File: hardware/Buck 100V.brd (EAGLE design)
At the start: 100 x 80 mm, 31 parts, among them M1 SI3430DV, M2 SI5435BDC, Q1 FMMT625, Q2 FMMT723, U1 LT3756EMSE

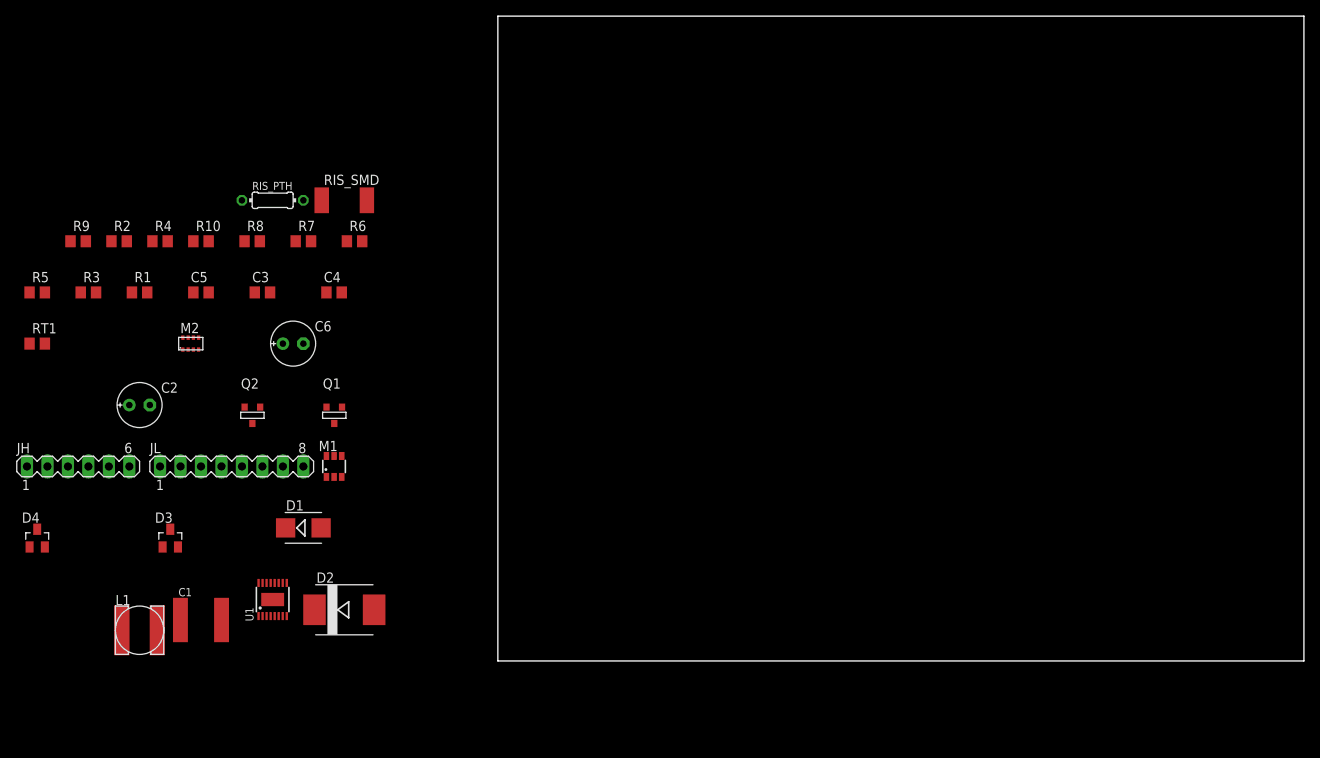
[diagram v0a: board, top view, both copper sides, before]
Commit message: Create kelvin terminated versions of current sense resistors and adjust schematic accordingly. Signals on the buck headers are now more clearly named. The kelvin terminated resistors WILL cause DRC errors on the board due to overlapping vias / pads but these can be safely ignored. Someday perhaps Eagle will get a better way to deal with kelvin termination.
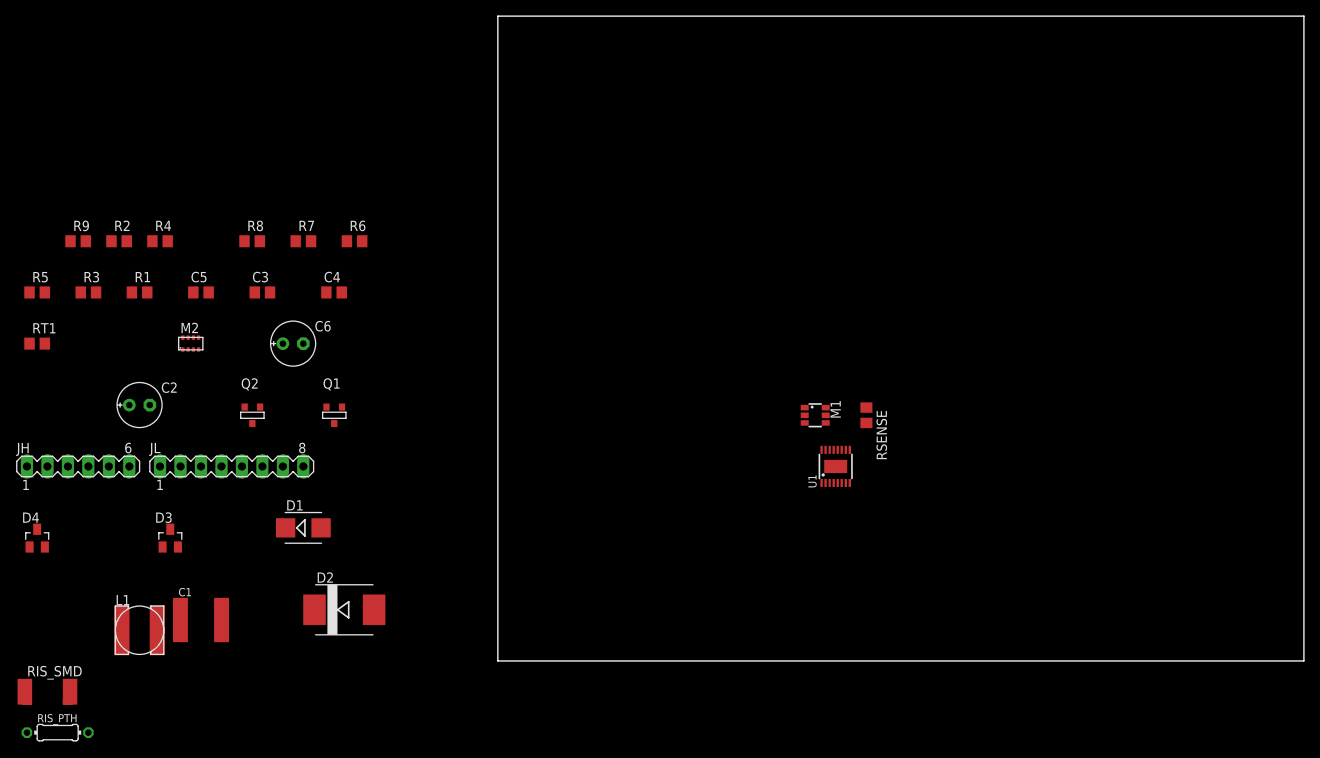
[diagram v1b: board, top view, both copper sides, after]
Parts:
- removed R10: 0.1, rcl:R0805
- added RSENSE: 0.1, rcl:R0805
- RIS_PTH: device rcl:0204/7 -> LED-drivers:0204/7-KELVIN
- RIS_SMD: device rcl:R2512 -> LED-drivers:R2512_KELVIN
- moved U1 71.8 mm to (41.9, 24.1)
- moved RIS_PTH 71.2 mm to (-54.6, -8.89)
- moved RIS_SMD 71.2 mm to (-55.9, -3.81)
- moved M1 60.0 mm to (39.4, 30.5), turned to 270 degrees
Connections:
- removed net IS: JH.3, M2.5, RIS_PTH.1, RIS_SMD.1, U1.3
- new net ISN: JH.3, RIS_PTH.1S, RIS_SMD.1S, U1.3
- new net ISP: JH.2, RIS_PTH.2S, RIS_SMD.2S, U1.4
- new net N$7: M2.5, RIS_PTH.1, RIS_SMD.1
- net GND: now also RSENSE.1; no longer R10.1
- net N$14: now also RSENSE.2; no longer R10.2
- net V+: no longer JH.2, U1.4

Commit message: Very rough initial board layout. Can now safely say that the board will be smaller than 2 inches by 3 inches.
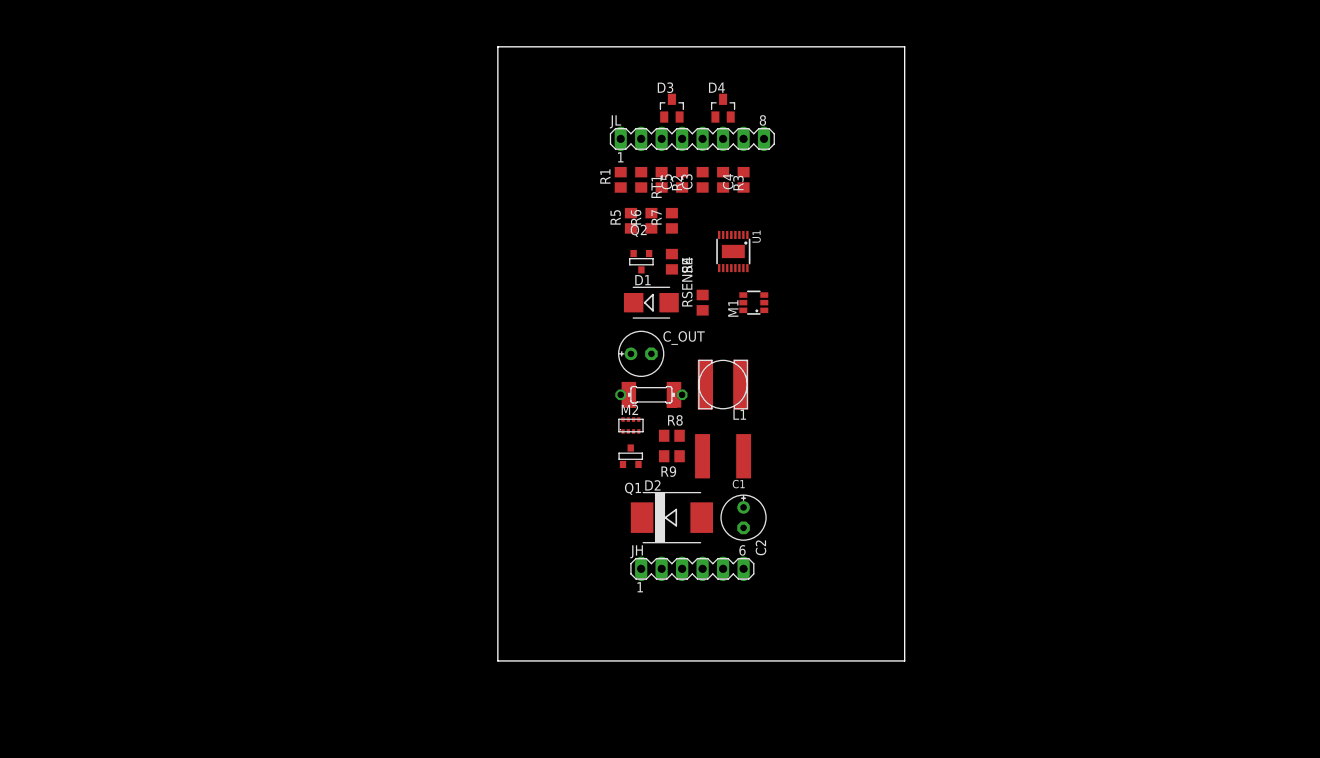
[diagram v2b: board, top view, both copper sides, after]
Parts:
- removed C6: 15uF 100V, rcl:E2,5-6E
- added C_OUT: 15uF 100V, rcl:E2,5-6E
- moved D4 100.4 mm to (27.9, 68.6)
- moved RIS_PTH 84.7 mm to (19.1, 33.0)
- moved RIS_SMD 83.5 mm to (19.1, 33.0)
- moved D3 82.0 mm to (21.6, 68.6)
- moved R3 80.0 mm to (27.9, 59.7), turned to 270 degrees
- moved L1 78.5 mm to (27.9, 34.3), turned to 180 degrees
- moved R9 78.3 mm to (21.6, 25.4), turned to 180 degrees
- moved RT1 77.6 mm to (17.8, 59.7), turned to 270 degrees
- moved JH 77.3 mm to (24.1, 11.4)
- moved C2 76.2 mm to (30.5, 17.8), turned to 270 degrees
- moved R5 74.2 mm to (16.5, 54.6), turned to 90 degrees
- moved JL 70.1 mm to (24.1, 64.8)
- moved C1 67.9 mm to (27.9, 25.4), turned to 180 degrees
- moved R2 67.7 mm to (20.3, 59.7), turned to 270 degrees
- moved R4 63.6 mm to (21.6, 49.5), turned to 270 degrees
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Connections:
- net N$12 renamed N_BUCK
- net LED_C: now also C_OUT.+; no longer C6.+
- net V+: now also C_OUT.-; no longer C6.-
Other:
- board size 100 x 80 mm -> 50.5 x 76.2 mm

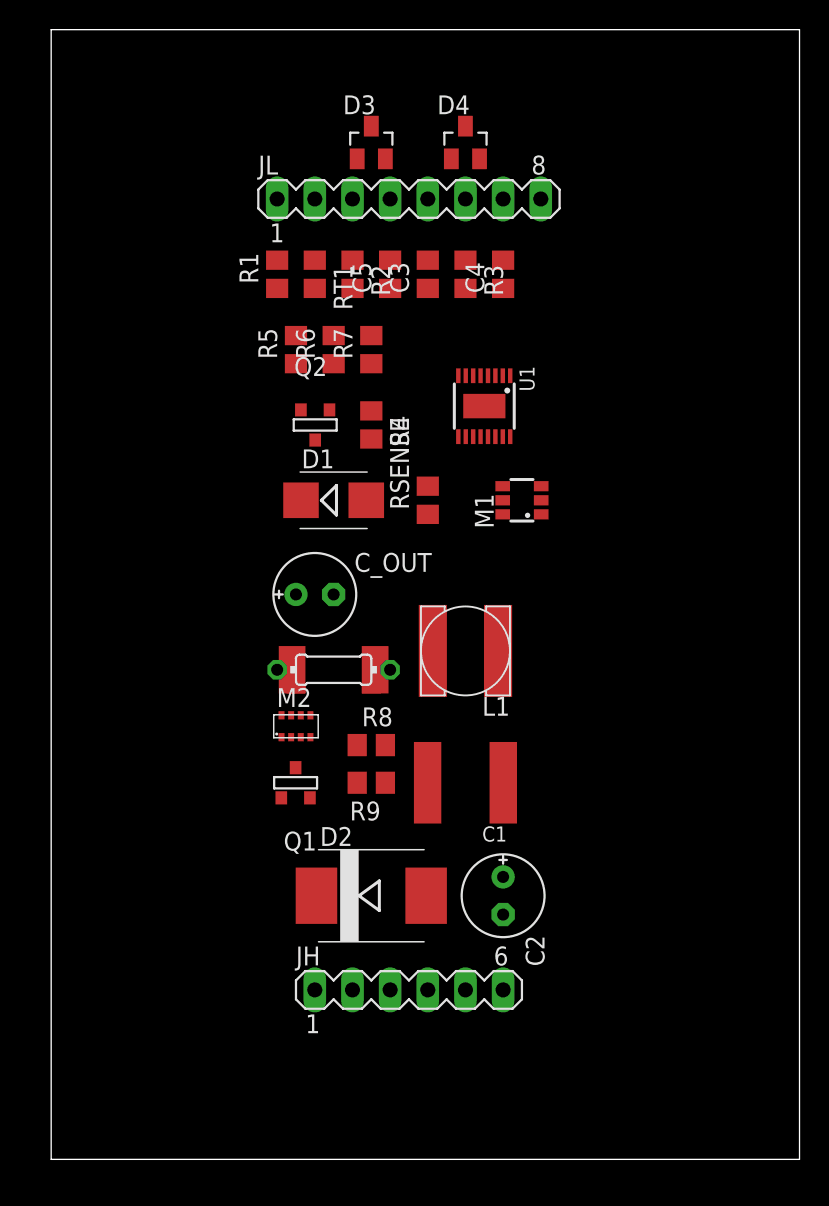
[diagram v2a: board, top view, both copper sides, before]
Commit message: Some progress on layout and routing.
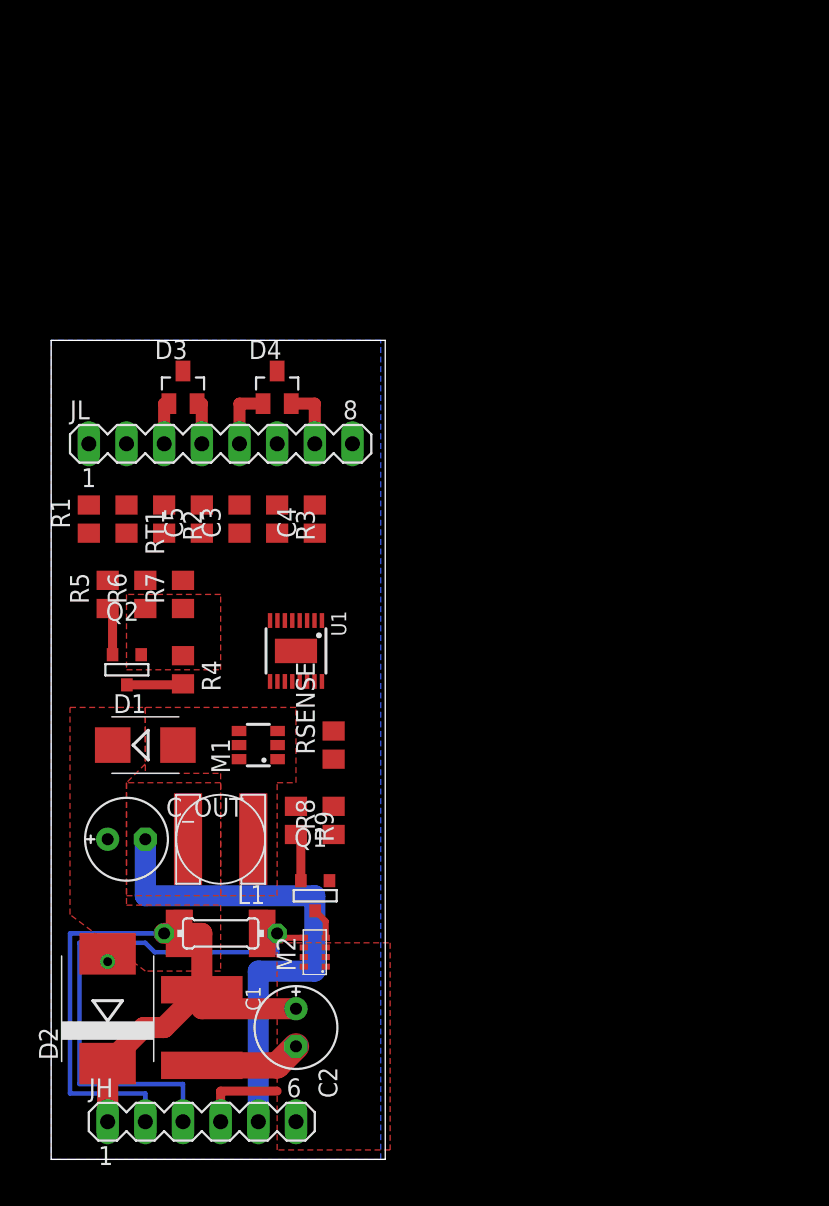
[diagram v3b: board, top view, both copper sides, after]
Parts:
- moved C1 24.3 mm to (10.2, 8.89), turned to 270 degrees
- moved M1 24.3 mm to (14.0, 27.9)
- moved C_OUT 20.8 mm to (5.08, 21.6)
- moved D1 20.8 mm to (6.35, 27.9)
- moved D4 20.8 mm to (15.2, 52.1)
- moved L1 20.8 mm to (11.4, 21.6)
- moved Q2 20.8 mm to (5.08, 33.0)
- moved R3 20.8 mm to (15.2, 43.2)
- moved R5 20.8 mm to (3.81, 38.1)
- moved R6 20.8 mm to (6.35, 38.1)
- moved RT1 20.8 mm to (5.08, 43.2)
- moved C3 20.8 mm to (12.7, 43.2)
- moved C4 20.8 mm to (17.8, 43.2)
- moved C5 20.8 mm to (10.2, 43.2)
- moved D3 20.8 mm to (8.89, 52.1)
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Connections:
- net LED_C: now also C_OUT.-; no longer C_OUT.+
- net V+: now also C_OUT.+; no longer C_OUT.-
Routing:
- net ISN: track 0.00 -> 36.5 mm
- net LED_C: track 0.00 -> 34.3 mm
- net ISP: track 0.00 -> 26.7 mm
- net V+: track 0.00 -> 26.3 mm
- net FB: track 0.00 -> 8.11 mm
- net GND: track 0.00 -> 7.41 mm, vias 0 -> 1
- net LED_A: track 0.00 -> 5.87 mm
- net CTRL: track 0.00 -> 4.30 mm
- net N$10: track 0.00 -> 3.25 mm
- net FB_TOP: track 0.00 -> 3.25 mm
- net N$7: track 0.00 -> 3.11 mm
- net PWM: track 0.00 -> 3.03 mm
- net /OPEN_LED: track 0.00 -> 3.03 mm
- net N$9: track 0.00 -> 2.11 mm
- added copper zone on layer 16, net GND
- added copper zone on layer 1, net LED_A
- added copper zone on layer 1, net LED_C
- added copper zone on layer 1, net N$8
- added copper zone on layer 1, net N_BUCK
- added copper zone on layer 1, net V+
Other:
- board size 50.5 x 76.2 mm -> 22.5 x 55.2 mm

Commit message: Progress on layout and routing.
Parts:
- moved M2 8.98 mm to (8.89, 12.7), turned to 180 degrees
- moved RIS_PTH 8.35 mm to (3.17, 14.0), turned to 90 degrees
- moved RIS_SMD 8.35 mm to (3.17, 14.0), turned to 90 degrees
- moved C1 8.13 mm to (16.5, 3.81), turned to 0 degrees
- moved JH 7.41 mm to (14.0, 8.89)
- moved D2 6.84 mm to (6.35, 3.81), turned to 0 degrees
- moved C2 5.12 mm to (19.1, 13.3), turned to 315 degrees
- moved L1 1.91 mm to (11.4, 19.7)
- moved M1 1.27 mm to (14.0, 26.7)
- moved R8 1.27 mm to (19.1, 21.6)
- moved R9 1.27 mm to (16.5, 21.6)
- moved RSENSE 1.27 mm to (19.1, 26.7)
- moved U1 0.63 mm to (16.5, 34.9)
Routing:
- net VREF: track 0.00 -> 43.8 mm, vias 0 -> 1
- net V+: track 26.3 -> 69.7 mm, vias 0 -> 4
- net N$11: track 0.00 -> 23.5 mm
- net FB_TOP: track 3.25 -> 24.6 mm, vias 0 -> 1
- net GND: track 7.41 -> 25.0 mm, vias 1 -> 13
- net FB: track 8.11 -> 24.4 mm
- net CTRL: track 4.30 -> 20.5 mm
- net N$14: track 0.00 -> 14.4 mm, vias 0 -> 2
- net N$9: track 2.11 -> 16.3 mm
- net LED_C: track 34.3 -> 47.6 mm, vias 0 -> 1
- net N$13: track 0.00 -> 7.02 mm
- net LED_A: track 5.87 -> 0.00 mm
- net ISN: track 36.5 -> 41.9 mm
- net N$7: track 3.11 -> 8.02 mm
- net ISP: track 26.7 -> 28.2 mm
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
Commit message: Checkpoint before trying autorouting again.
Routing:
- net FB: track 24.4 -> 44.5 mm, vias 0 -> 2
- net ISN: track 41.9 -> 51.8 mm, vias 0 -> 1
- net ISP: track 28.2 -> 37.0 mm, vias 0 -> 1
- net V+: track 69.7 -> 74.2 mm
- net LED_C: track 47.6 -> 50.8 mm
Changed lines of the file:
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@@
 <polygon width="0.4064" layer="1" thermals="no" rank="3">
 <vertex x="7.62" y="40.005"/>
-<vertex x="7.62" y="25.4"/>
-<vertex x="5.08" y="25.4"/>
+<vertex x="7.62" y="24.765"/>
+<vertex x="5.08" y="24.765"/>
 <vertex x="5.08" y="13.335"/>
 <vertex x="0" y="13.335"/>
@@
 <vertex x="13.97" y="15.875"/>
 </polygon>
+<wire x1="3.81" y1="21.59" x2="3.175" y2="21.59" width="1.6764" layer="1"/>
+<wire x1="3.175" y1="21.59" x2="3.175" y2="17.78" width="1.6764" layer="1"/>
 </signal>
 <signal name="SHDN">
@@
 <wire x1="21.2725" y1="38.1" x2="17.76" y2="38.1" width="0.3048" layer="1"/>
 <wire x1="17.76" y1="38.1" x2="17.76" y2="36.975" width="0.3048" layer="1"/>
-<wire x1="8.89" y1="32.07" x2="17.76" y2="36.975" width="0" layer="19" extent="1-1"/>
+<wire x1="8.89" y1="32.07" x2="11.115" y2="29.845" width="0.3048" layer="1"/>
+<wire x1="11.115" y1="29.845" x2="12.7" y2="29.845" width="0.3048" layer="1"/>
+<via x="12.7" y="29.845" extent="1-16" drill="0.6"/>
+<wire x1="12.7" y1="29.845" x2="19.3675" y2="29.845" width="0.3048" layer="16"/>
+<wire x1="19.3675" y1="29.845" x2="19.3675" y2="35.2425" width="0.3048" layer="16"/>
+<via x="19.3675" y="35.2425" extent="1-16" drill="0.6"/>
+<wire x1="19.3675" y1="35.2425" x2="19.3675" y2="36.068" width="0.254" layer="1"/>
+<wire x1="19.3675" y1="36.068" x2="17.78" y2="36.068" width="0.254" layer="1"/>
+<wire x1="17.78" y1="36.975" x2="17.78" y2="36.068" width="0.254" layer="1"/>
+<wire x1="17.78" y1="36.975" x2="17.76" y2="36.975" width="0" layer="19" extent="1-1"/>
 </signal>
 <signal name="FB_TOP">
@@
 <wire x1="10.4775" y1="39.05" x2="10.4775" y2="39.0525" width="0.3048" layer="1"/>
 <via x="10.4775" y="39.0525" extent="1-16" drill="0.6"/>
-<wire x1="10.4775" y1="39.0525" x2="2.8575" y2="39.0525" width="0.3048" layer="16"/>
-<wire x1="2.8575" y1="39.0525" x2="2.8575" y2="23.8125" width="0.3048" layer="16"/>
-<wire x1="2.8575" y1="23.8125" x2="6.35" y2="23.8125" width="0.3048" layer="16"/>
+<wire x1="10.4775" y1="39.0525" x2="1.27" y2="39.0525" width="0.3048" layer="16"/>
+<wire x1="1.27" y1="39.0525" x2="1.27" y2="23.8125" width="0.3048" layer="16"/>
+<wire x1="1.27" y1="23.8125" x2="6.35" y2="23.8125" width="0.3048" layer="16"/>
 <wire x1="6.35" y1="23.8125" x2="6.35" y2="21.59" width="0.3048" layer="16"/>
 </signal>
@@
 <wire x1="8.89" y1="12.065" x2="3.175" y2="17.78" width="0.3048" layer="16"/>
 <wire x1="4.445" y1="16.51" x2="3.175" y2="17.78" width="0.3048" layer="1"/>
-<wire x1="3.175" y1="17.78" x2="3.175" y2="18.0975" width="0.254" layer="16"/>
-<wire x1="3.175" y1="18.0975" x2="1.905" y2="19.3675" width="0.254" layer="16"/>
-<wire x1="1.905" y1="19.3675" x2="1.905" y2="31.115" width="0.254" layer="16"/>
-<wire x1="1.905" y1="31.115" x2="16.76" y2="36.975" width="0" layer="19" extent="1-16"/>
+<wire x1="3.175" y1="17.78" x2="1.905" y2="17.78" width="0.254" layer="1"/>
+<wire x1="1.905" y1="17.78" x2="1.905" y2="29.5275" width="0.254" layer="1"/>
+<wire x1="1.905" y1="29.5275" x2="2.2225" y2="29.845" width="0.254" layer="1"/>
+<via x="2.2225" y="29.845" extent="1-16" drill="0.6"/>
+<wire x1="2.2225" y1="29.845" x2="11.43" y2="29.845" width="0.254" layer="16"/>
+<wire x1="11.43" y1="29.845" x2="16.76" y2="36.975" width="0" layer="19" extent="1-16"/>
 </signal>
 <signal name="N$7">
@@
 <wire x1="3.175" y1="10.16" x2="4.445" y2="10.16" width="0.3048" layer="1"/>
 <wire x1="4.445" y1="10.16" x2="4.445" y2="11.43" width="0.3048" layer="1"/>
-<wire x1="3.175" y1="10.16" x2="1.27" y2="10.16" width="0.254" layer="16"/>
-<wire x1="1.27" y1="10.16" x2="1.27" y2="31.75" width="0.254" layer="16"/>
-<wire x1="3.175" y1="6.35" x2="3.175" y2="10.16" width="0.3048" layer="1"/>
-<wire x1="1.27" y1="31.75" x2="17.26" y2="36.975" width="0" layer="19" extent="1-16"/>
+<wire x1="3.175" y1="10.16" x2="1.27" y2="10.16" width="0.254" layer="1"/>
+<wire x1="1.27" y1="10.16" x2="1.27" y2="31.115" width="0.254" layer="1"/>
+<wire x1="1.27" y1="31.115" x2="2.2225" y2="31.115" width="0.254" layer="1"/>
+<via x="2.2225" y="31.115" extent="1-16" drill="0.6"/>
+<wire x1="2.2225" y1="31.115" x2="11.7475" y2="31.115" width="0.254" layer="16"/>
+<wire x1="11.7475" y1="31.115" x2="17.26" y2="36.975" width="0" layer="19" extent="1-16"/>
+<wire x1="3.175" y1="10.16" x2="3.175" y2="6.35" width="0.254" layer="1"/>
 </signal>
 </signals>

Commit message: VICTORY! Over place and route.
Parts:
- moved R3 10.6 mm to (14.5, 32.6), turned to 90 degrees
- moved C3 10.6 mm to (12.1, 32.6), turned to 270 degrees
- moved C4 10.6 mm to (17.9, 32.6), turned to 270 degrees
- moved U1 3.10 mm to (16.5, 38.0)
- moved JH 0.71 mm to (14.0, 8.18)
- moved JL 0.56 mm to (11.4, 48.8)
- moved D4 0.33 mm to (15.3, 52.4)
- moved D3 0.32 mm to (8.89, 52.4)
- moved C1 0.08 mm to (16.5, 3.73)
- moved D2 0.08 mm to (6.35, 3.73)
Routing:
- net SHDN: track 0.00 -> 39.3 mm, vias 0 -> 2
- net ISP: track 37.0 -> 64.6 mm, vias 1 -> 2
- net ISN: track 51.8 -> 74.6 mm, vias 1 -> 2
- net /OPEN_LED: track 3.03 -> 24.9 mm
- net CTRL: track 20.5 -> 42.3 mm, vias 0 -> 2
- net N$3: track 0.00 -> 16.3 mm, vias 0 -> 2
- net PWM: track 3.03 -> 18.5 mm, vias 0 -> 1
- net VREF: track 43.8 -> 32.2 mm
- net N$13: track 7.02 -> 14.1 mm
- net N$14: track 14.4 -> 21.4 mm
- net N$1: track 0.00 -> 4.64 mm
- net N$4: track 0.00 -> 4.45 mm
- net GND: track 25.0 -> 28.3 mm, vias 13 -> 17
- net V+: track 74.2 -> 77.3 mm
- net N$11: track 23.5 -> 26.6 mm
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- added copper zone on layer 1, net GND
